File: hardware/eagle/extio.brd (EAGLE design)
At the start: 66 x 52 mm, 52 parts, among them IC1 PCF8574P, Q1 IRLZ44N, Q2 IRLZ44N, Q3 IRLZ44N, Q4 IRLZ44N, Q5 IRLZ44N, Q6 IRLZ44N, Q7 IRLZ44N, Q8 IRLZ44N

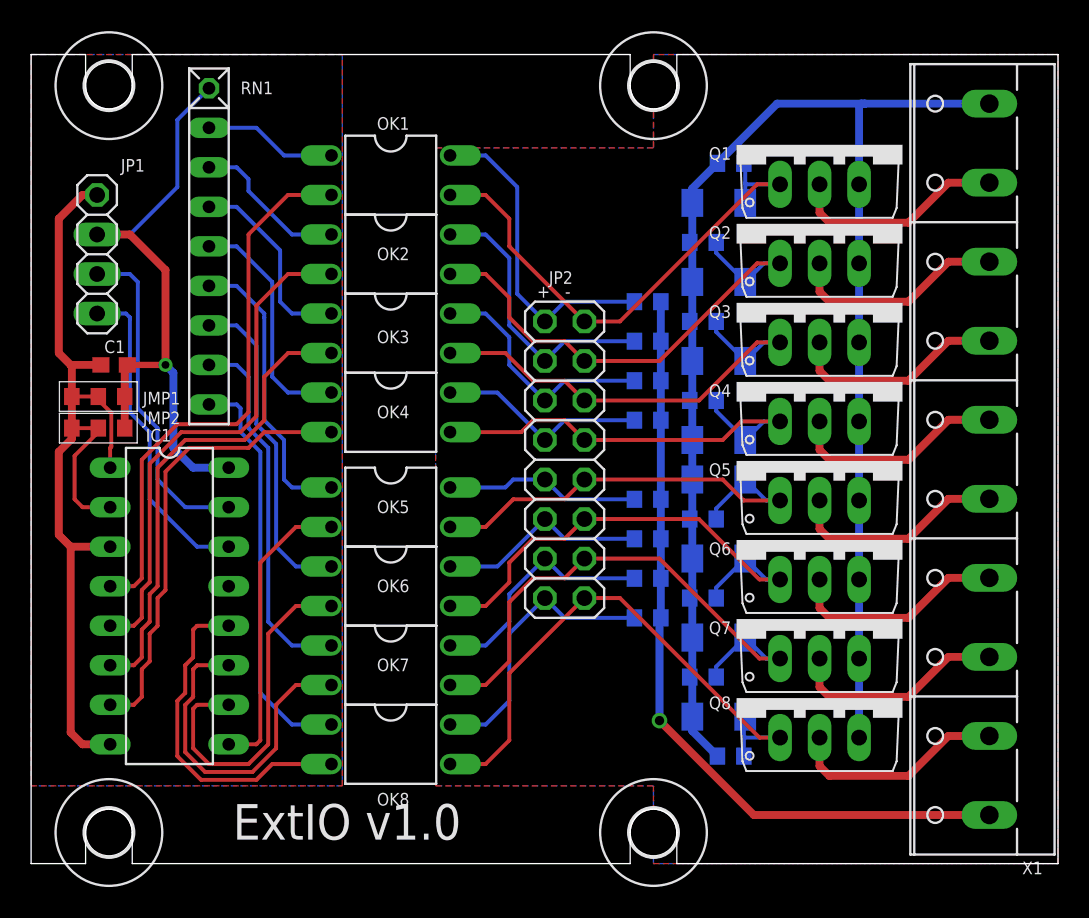
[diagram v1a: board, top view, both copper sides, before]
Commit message: ExtIO: GND fix, JP1 via via :)
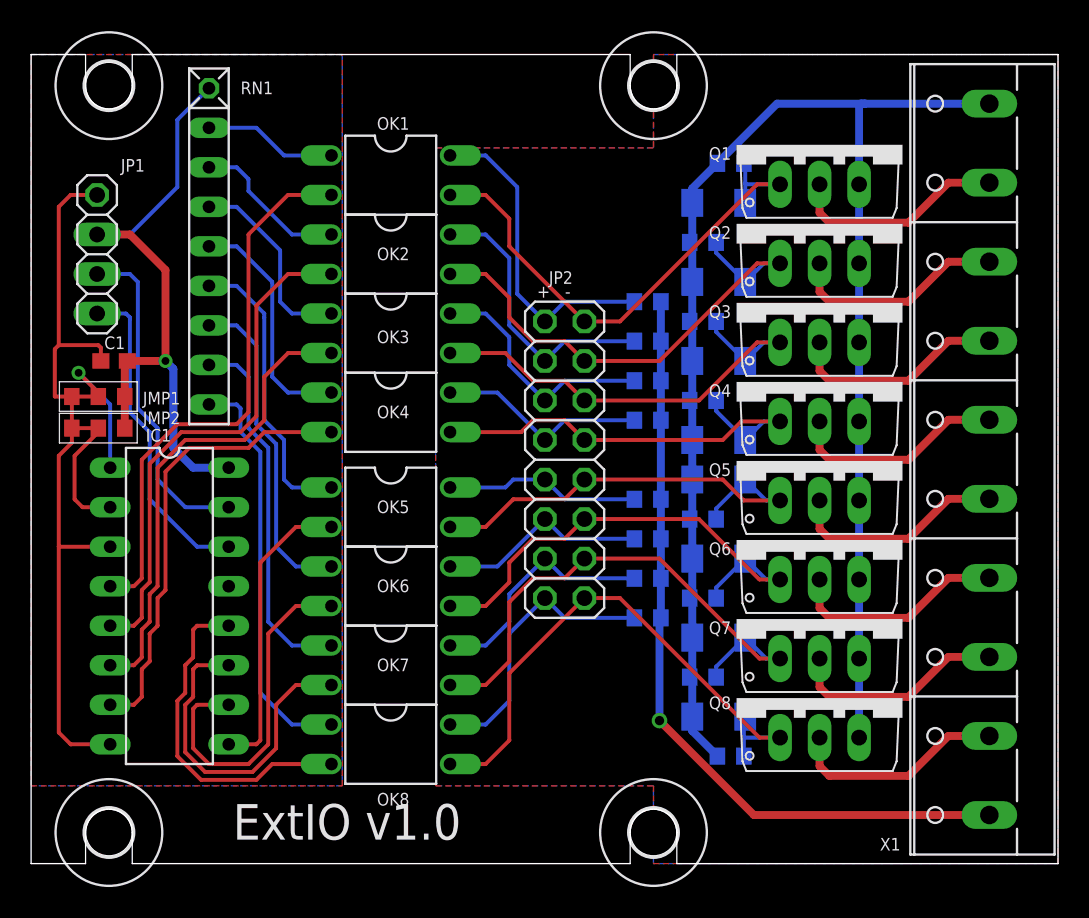
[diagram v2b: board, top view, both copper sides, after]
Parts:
- moved C1 0.25 mm to (5.33, 35.3)
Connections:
- net N$1 renamed GND
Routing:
- net GND: track 44.5 -> 48.7 mm
- net N$2: track 4.96 -> 8.99 mm, vias 0 -> 1
- added copper zone on layer 1, net GND
- added copper zone on layer 16, net GND
- removed copper zone on layer 1, net N$71
- removed copper zone on layer 16, net N$71
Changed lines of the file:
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@@
 <attribute name="OC_NEWARK" value="unknown" x="60.952" y="28.984" size="1.778" layer="27" rot="R90" display="off"/>
 <attribute name="VALUE" x="65.27" y="4.854" size="1.524" layer="27" ratio="10" rot="R90"/>
-<attribute name="NAME" x="65.02" y="3.128" size="0.8128" layer="25" font="vector" ratio="10" rot="R180"/>
+<attribute name="NAME" x="55.876" y="4.652" size="0.8128" layer="25" font="vector" ratio="10" rot="R180"/>
 </element>
 <element name="JP2" library="gate433" package="2X08" value="" x="34.29" y="28.956" smashed="yes" rot="R270">
@@
 <element name="U$3" library="gate433" package="3,0" value="" x="40" y="5" locked="yes" smashed="yes"/>
 <element name="U$4" library="gate433" package="3,0" value="" x="40" y="53" locked="yes" smashed="yes"/>
-<element name="C1" library="resistor" package="C0603" value="1uF" x="5.334" y="35.052" smashed="yes" rot="R180">
-<attribute name="NAME" x="4.699" y="35.814" size="0.8128" layer="25" font="vector" ratio="10"/>
-<attribute name="VALUE" x="3.175" y="36.957" size="1.27" layer="27" ratio="10" rot="R180"/>
-<attribute name="SPICEPREFIX" value="C" x="5.334" y="35.052" size="1.778" layer="27" rot="R180" display="off"/>
+<element name="C1" library="resistor" package="C0603" value="1uF" x="5.334" y="35.306" smashed="yes" rot="R180">
+<attribute name="NAME" x="4.699" y="36.068" size="0.8128" layer="25" font="vector" ratio="10"/>
+<attribute name="VALUE" x="3.175" y="37.211" size="1.27" layer="27" ratio="10" rot="R180"/>
+<attribute name="SPICEPREFIX" value="C" x="5.334" y="35.306" size="1.778" layer="27" rot="R180" display="off"/>
 </element>
 <element name="JMP1" library="gate433" package="JMP0603-ACLOSED" value="0R-JUMP0603-ACLOSED" x="4.318" y="33.02" smashed="yes">
@@
 <wire x1="12.7" y1="28.448" x2="10.414" y2="28.448" width="0.508" layer="16"/>
 <wire x1="10.414" y1="28.448" x2="9.144" y2="29.718" width="0.508" layer="16"/>
-<wire x1="9.144" y1="29.718" x2="9.144" y2="34.544" width="0.508" layer="16"/>
-<wire x1="9.144" y1="34.544" x2="8.636" y2="35.052" width="0.508" layer="16"/>
-<via x="8.636" y="35.052" extent="1-16" drill="0.5"/>
-<wire x1="8.636" y1="35.052" x2="8.636" y2="41.148" width="0.508" layer="1"/>
+<wire x1="9.144" y1="29.718" x2="9.144" y2="34.798" width="0.508" layer="16"/>
+<wire x1="9.144" y1="34.798" x2="8.636" y2="35.306" width="0.508" layer="16"/>
+<via x="8.636" y="35.306" extent="1-16" drill="0.5"/>
+<wire x1="8.636" y1="35.306" x2="8.636" y2="41.148" width="0.508" layer="1"/>
 <wire x1="8.636" y1="41.148" x2="6.35" y2="43.434" width="0.508" layer="1"/>
 <wire x1="6.35" y1="43.434" x2="4.2418" y2="43.434" width="0.508" layer="1"/>
-<wire x1="6.184" y1="35.052" x2="8.636" y2="35.052" width="0.4064" layer="1"/>
+<wire x1="6.184" y1="35.306" x2="8.636" y2="35.306" width="0.508" layer="1"/>
 <contactref element="JMP2" pad="B"/>
 <contactref element="JMP1" pad="B"/>
 <wire x1="6.018" y1="30.988" x2="6.018" y2="33.02" width="0.508" layer="1"/>
-<wire x1="6.018" y1="33.02" x2="6.018" y2="34.886" width="0.508" layer="1"/>
-<wire x1="6.018" y1="34.886" x2="6.184" y2="35.052" width="0.508" layer="1"/>
-</signal>
-<signal name="N$71">
+<wire x1="6.018" y1="33.02" x2="6.018" y2="35.14" width="0.508" layer="1"/>
+<wire x1="6.018" y1="35.14" x2="6.184" y2="35.306" width="0.508" layer="1"/>
+</signal>
+<signal name="GND">
+<contactref element="JP1" pad="1"/>
+<contactref element="C1" pad="2"/>
+<contactref element="JMP1" pad="A"/>
+<contactref element="IC1" pad="8"/>
+<contactref element="JMP2" pad="A"/>
+<contactref element="IC1" pad="3"/>
+<polygon width="0.4064" layer="1" isolate="0.6096">
+<vertex x="20" y="55"/>
+<vertex x="0" y="55"/>
+<vertex x="0" y="8"/>
+<vertex x="20" y="8"/>
+</polygon>
+<wire x1="4.2418" y1="45.974" x2="2.54" y2="45.974" width="0.254" layer="1"/>
+<wire x1="2.54" y1="45.974" x2="1.778" y2="45.212" width="0.254" layer="1"/>
+<wire x1="1.778" y1="45.212" x2="1.778" y2="36.322" width="0.254" layer="1"/>
+<wire x1="1.778" y1="36.322" x2="4.318" y2="36.322" width="0.254" layer="1"/>
+<wire x1="4.318" y1="36.322" x2="4.484" y2="36.156" width="0.254" layer="1"/>
+<wire x1="4.484" y1="36.156" x2="4.484" y2="35.306" width="0.254" layer="1"/>
+<wire x1="2.618" y1="33.02" x2="2.618" y2="30.988" width="0.254" layer="1"/>
+<wire x1="2.618" y1="33.02" x2="1.524" y2="33.02" width="0.254" layer="1"/>
+<wire x1="1.524" y1="33.02" x2="1.524" y2="36.068" width="0.254" layer="1"/>
+<wire x1="1.524" y1="36.068" x2="1.778" y2="36.322" width="0.254" layer="1"/>
+<wire x1="2.618" y1="30.988" x2="2.618" y2="30.05" width="0.254" layer="1"/>
+<wire x1="2.618" y1="30.05" x2="1.778" y2="29.21" width="0.254" layer="1"/>
+<wire x1="1.778" y1="29.21" x2="1.778" y2="23.368" width="0.254" layer="1"/>
+<wire x1="1.778" y1="23.368" x2="1.778" y2="11.43" width="0.254" layer="1"/>
+<wire x1="1.778" y1="11.43" x2="2.54" y2="10.668" width="0.254" layer="1"/>
+<wire x1="2.54" y1="10.668" x2="5.08" y2="10.668" width="0.254" layer="1"/>
+<wire x1="5.08" y1="23.368" x2="1.778" y2="23.368" width="0.254" layer="1"/>
 <polygon width="0.4064" layer="16" isolate="0.6096">
 <vertex x="0" y="55"/>
@@
 <vertex x="0" y="8"/>
 </polygon>
-<polygon width="0.4064" layer="1" isolate="0.6096">
-<vertex x="20" y="55"/>
-<vertex x="0" y="55"/>
-<vertex x="0" y="8"/>
-<vertex x="20" y="8"/>
-</polygon>
-</signal>
-<signal name="N$1">
-<contactref element="JP1" pad="1"/>
-<contactref element="C1" pad="2"/>
-<contactref element="JMP1" pad="A"/>
-<contactref element="IC1" pad="8"/>
-<contactref element="JMP2" pad="A"/>
-<contactref element="IC1" pad="3"/>
-<wire x1="4.2418" y1="45.974" x2="3.302" y2="45.974" width="0.508" layer="1"/>
-<wire x1="3.302" y1="45.974" x2="1.778" y2="44.45" width="0.508" layer="1"/>
-<wire x1="1.778" y1="44.45" x2="1.778" y2="35.814" width="0.508" layer="1"/>
-<wire x1="1.778" y1="35.814" x2="2.54" y2="35.052" width="0.508" layer="1"/>
-<wire x1="2.54" y1="35.052" x2="4.484" y2="35.052" width="0.508" layer="1"/>
-<wire x1="2.618" y1="33.02" x2="2.618" y2="34.974" width="0.508" layer="1"/>
-<wire x1="2.618" y1="34.974" x2="2.54" y2="35.052" width="0.508" layer="1"/>
-<wire x1="2.618" y1="30.988" x2="2.618" y2="33.02" width="0.508" layer="1"/>
-<wire x1="2.618" y1="30.988" x2="2.618" y2="30.304" width="0.508" layer="1"/>
-<wire x1="2.618" y1="30.304" x2="1.778" y2="29.464" width="0.508" layer="1"/>
-<wire x1="1.778" y1="29.464" x2="1.778" y2="24.13" width="0.508" layer="1"/>
-<wire x1="5.08" y1="10.668" x2="3.302" y2="10.668" width="0.508" layer="1"/>
-<wire x1="3.302" y1="10.668" x2="2.54" y2="11.43" width="0.508" layer="1"/>
-<wire x1="2.54" y1="11.43" x2="2.54" y2="23.368" width="0.508" layer="1"/>
-<wire x1="1.778" y1="24.13" x2="2.54" y2="23.368" width="0.508" layer="1"/>
-<wire x1="5.08" y1="23.368" x2="2.54" y2="23.368" width="0.508" layer="1"/>
 </signal>
 <signal name="N$2">
 <contactref element="JMP1" pad="C"/>
 <contactref element="IC1" pad="1"/>
-<wire x1="4.318" y1="33.02" x2="4.318" y2="32.7914" width="0.254" layer="1"/>
-<wire x1="4.318" y1="32.7914" x2="5.1562" y2="31.9786" width="0.254" layer="1"/>
-<wire x1="5.1562" y1="31.9786" x2="5.1562" y2="29.7942" width="0.254" layer="1"/>
-<wire x1="5.1562" y1="29.7942" x2="5.08" y2="29.718" width="0.254" layer="1"/>
-<wire x1="5.08" y1="29.718" x2="5.08" y2="28.448" width="0.254" layer="1"/>
+<wire x1="4.318" y1="33.02" x2="4.318" y2="33.274" width="0.254" layer="1"/>
+<wire x1="4.318" y1="33.274" x2="3.048" y2="34.544" width="0.254" layer="1"/>
+<via x="3.048" y="34.544" extent="1-16" drill="0.5"/>
+<wire x1="3.048" y1="34.544" x2="5.08" y2="32.512" width="0.254" layer="16"/>
+<wire x1="5.08" y1="32.512" x2="5.08" y2="28.448" width="0.254" layer="16"/>
 </signal>
 <signal name="N$3">
